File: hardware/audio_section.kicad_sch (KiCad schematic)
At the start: 15 parts, among them J5 AudioJack3_SwitchTR, U2 WAU8812, U8 LM4875

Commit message: Finished power section
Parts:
- removed U8: LM4875, Package_SO:SOIC-8_3.9x4.9mm_P1.27mm, symbol newsymbols:LM4875
- added U10: LM4875, Package_SO:SOIC-8_3.9x4.9mm_P1.27mm, symbol additional_symbols:LM4875
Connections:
- net +5V: now also U10.1 (VDD)
- net GND: now also U10.6 (GND)
- net SPEAKER +: now also U10.5 (Vo1)
- net SPEAKER -: now also U10.8 (Vo2)
- net Volume control: now also U10.4 (DC_vol/~{SD})
- net at R11.1, R12.1, R13.1: now also U10.2 (-Vin)
- net at R15.2: now also U10.3 (HP_Sense)
- net at C17.1: now also U10.7 (Bypass)
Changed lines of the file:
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@@
 	)
 	(symbol
-		(lib_id "newsymbols:LM4875")
+		(lib_id "additional_symbols:LM4875")
 		(at 124.46 67.31 0)
 		(unit 1)
@@
 		(on_board yes)
 		(dnp no)
-		(property "Reference" "U8"
-			(at 128.27 64.77 0)
+		(fields_autoplaced yes)
+		(property "Reference" "U10"
+			(at 122.7933 64.77 0)
 			(effects
 				(font
 					(size 1.27 1.27)
 				)
+				(justify left)
 			)
 		)
 		(property "Value" "LM4875"
-			(at 130.81 67.31 0)
+			(at 122.7933 67.31 0)
 			(effects
 				(font
 					(size 1.27 1.27)
 				)
+				(justify left)
 			)
 		)
 		(property "Footprint" "Package_SO:SOIC-8_3.9x4.9mm_P1.27mm"
-			(at 124.46 64.77 0)
+			(at 121.158 49.53 0)
 			(effects
 				(font
@@
 		)
 		(property "Datasheet" "https://www.ti.com/lit/ds/symlink/lm4875.pdf"
-			(at 124.46 62.23 0)
+			(at 121.158 46.99 0)
 			(effects
 				(font
@@
 			)
 		)
-		(property "Description" ""
-			(at 124.46 67.31 0)
+		(property "Description" "750 mW Audio Power Amplifier with DC Volume Control and Headphone Switch"
+			(at 121.158 52.07 0)
 			(effects
 				(font
 					(size 1.27 1.27)
 				)
+				(hide yes)
 			)
 		)
-		(pin "4"
+		(pin "5"
+		)
+		(pin "8"
 		)
 		(pin "3"
-		)
-		(pin "1"
-		)
-		(pin "2"
-		)
-		(pin "5"
 		)
 		(pin "6"
@@
 		(pin "7"
 		)
-		(pin "8"
+		(pin "2"
+		)
+		(pin "4"
+		)
+		(pin "1"
 		)
 		(instances
-			(project "pyheld_pcb"
+			(project ""
 				(path "/ba6f8fdb-f4fe-4618-8996-8010efc6ab22/1cc4485c-21de-4da4-8687-5322240d5e0f"
-					(reference "U8")
+					(reference "U10")
 					(unit 1)
 				)

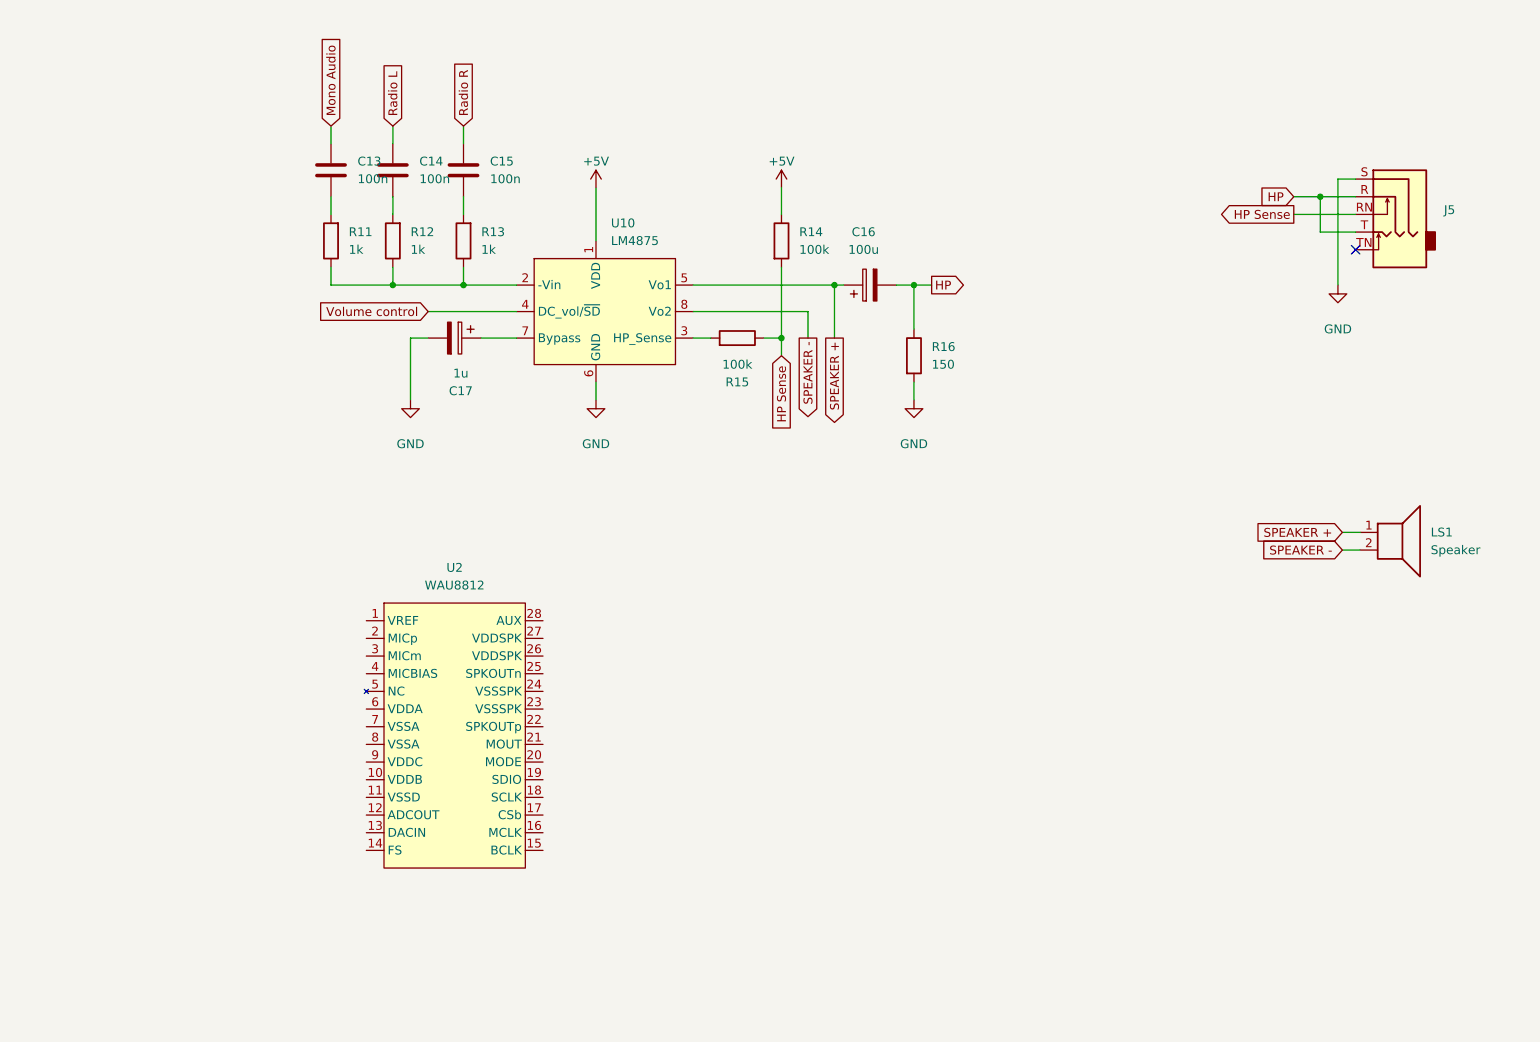
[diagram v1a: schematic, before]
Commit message: Moved MCU to general section
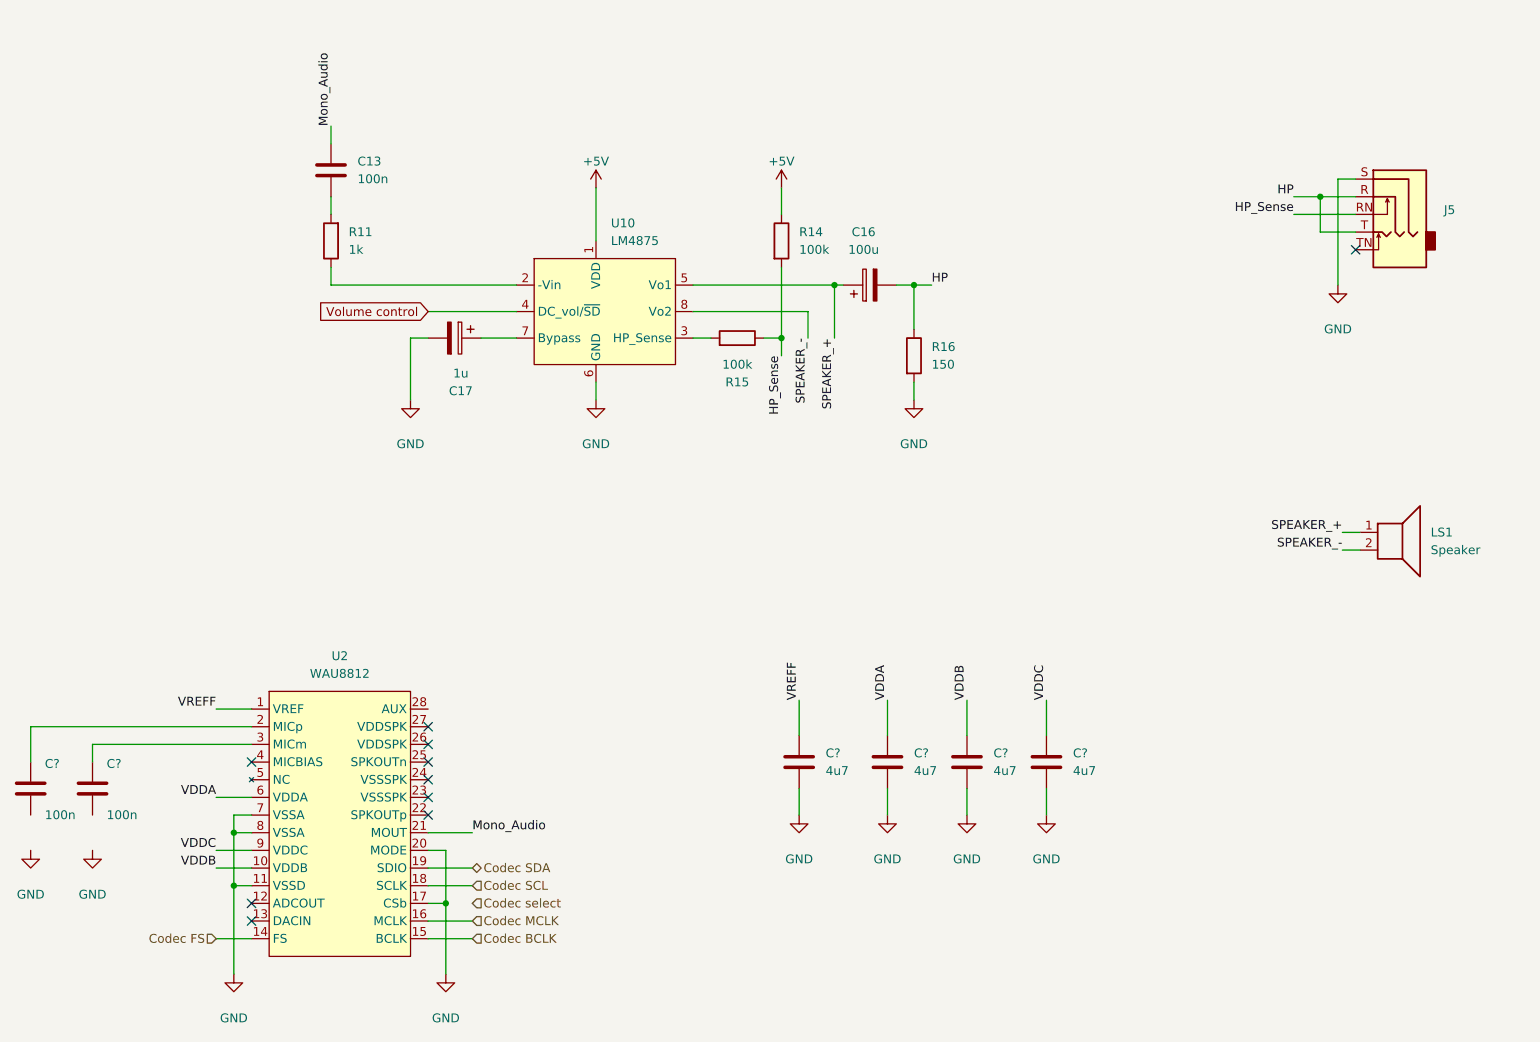
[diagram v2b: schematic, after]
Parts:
- removed C14, C15: 100n, Capacitor_SMD:C_0603_1608Metric, symbol Device:C
- removed R12, R13: 1k, Resistor_SMD:R_0603_1608Metric, symbol Device:R
- added C? (x4): 4u7, Capacitor_SMD:C_0603_1608Metric, symbol Device:C
- added C? (x2): 100n, Capacitor_SMD:C_0603_1608Metric, symbol Device:C
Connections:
- net Mono Audio is gone; now on net Mono_Audio: C13.2
- net GND: now also U2.11 (VSSD), U2.17 (CSb), U2.20 (MODE), U2.7 (VSSA), U2.8 (VSSA), C?.1, C?.1, C?.1, C?.1
- net VREFF: now reaches U2.1 (VREF)
- net VREFF: now also C?.2
- net VDDB: now reaches U2.10 (VDDB)
- net VDDB: now also C?.2
- net Codec FS: now reaches U2.14 (FS)
- net Codec BCLK: now reaches U2.15 (BCLK)
- net Codec MCLK: now reaches U2.16 (MCLK)
- net Codec SCL: now reaches U2.18 (SCLK)
- net Codec SDA: now reaches U2.19 (SDIO)
- net at U2.2 (MICp): now also C?.2
- net Mono_Audio: now reaches U2.21 (MOUT)
- net at U2.3 (MICm): now also C?.2
- net VDDA: now reaches U2.6 (VDDA)
- net VDDA: now also C?.2
- net VDDC: now reaches U2.9 (VDDC)
- net VDDC: now also C?.2
- net HP Sense renamed HP_Sense
- net SPEAKER + renamed SPEAKER_+
- net SPEAKER - renamed SPEAKER_-
- no-connect marks 1 -> 10
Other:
- moved on the sheet: U2

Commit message: Removed additional audio circuits Simplified connections -> change DAC (WAU8812 will be difficult by now to make working)
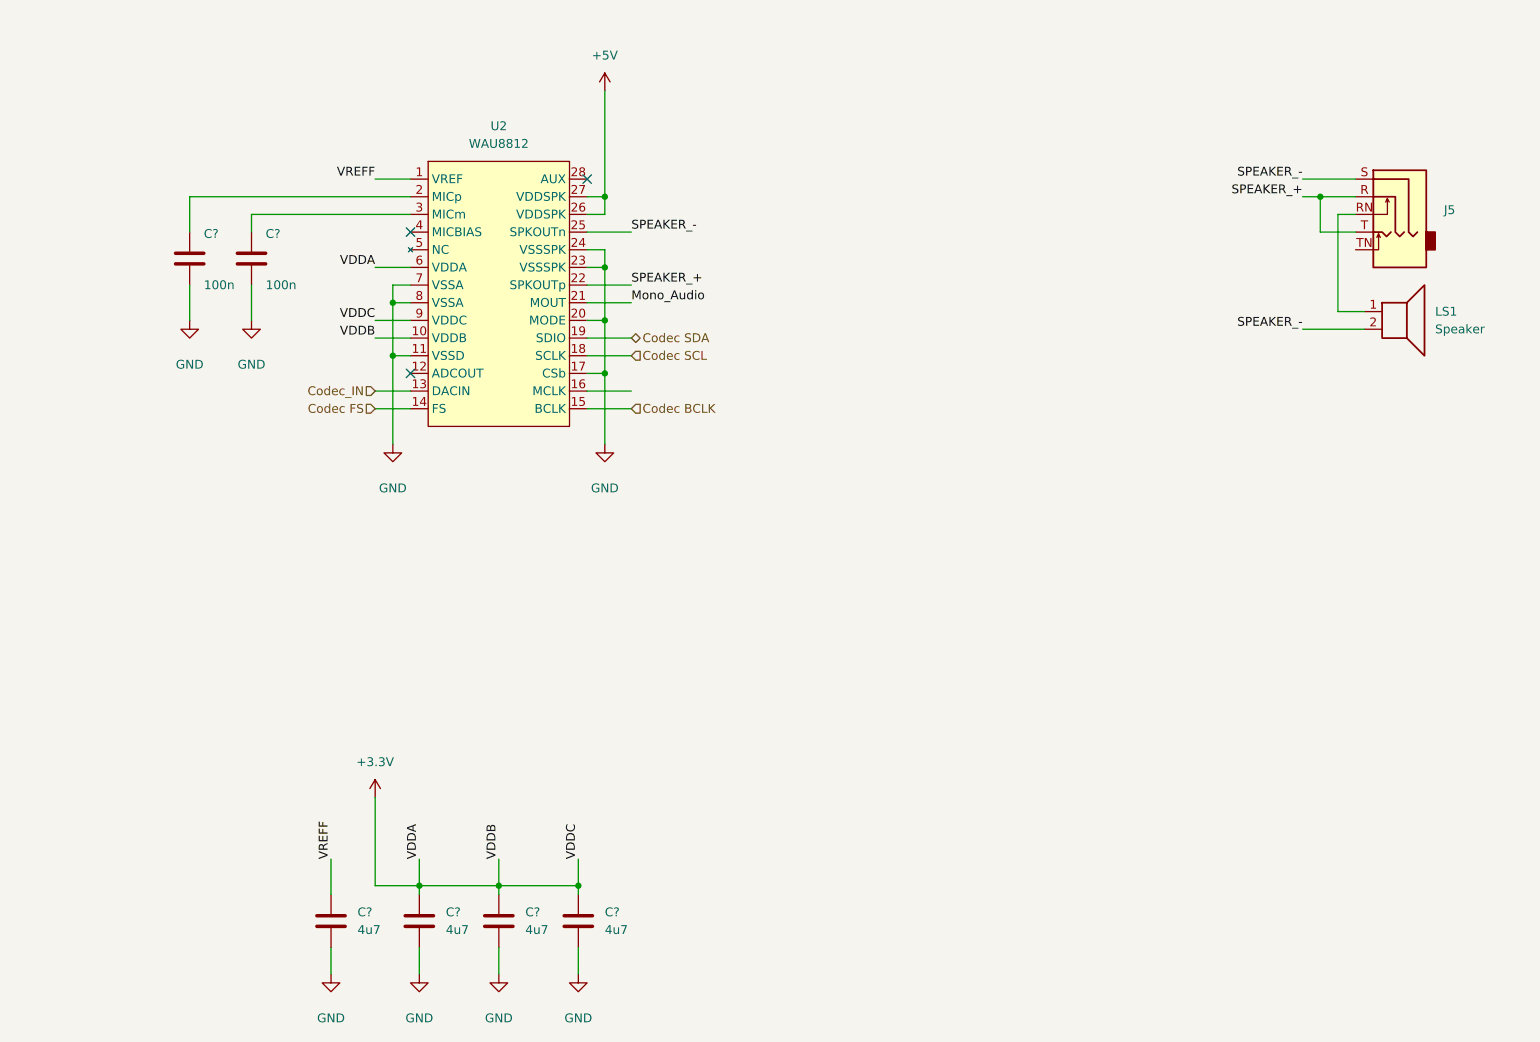
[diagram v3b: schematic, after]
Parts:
- removed C13: 100n, Capacitor_SMD:C_0603_1608Metric, symbol Device:C
- removed C16: 100u, Capacitor_SMD:C_0603_1608Metric, symbol Device:C_Polarized
- removed C17: 1u, Capacitor_SMD:C_0603_1608Metric, symbol Device:C_Polarized
- removed R11: 1k, Resistor_SMD:R_0603_1608Metric, symbol Device:R
- removed R14, R15: 100k, Resistor_SMD:R_0603_1608Metric, symbol Device:R
- removed R16: 150, Resistor_SMD:R_0603_1608Metric, symbol Device:R
- removed U10: LM4875, Package_SO:SOIC-8_3.9x4.9mm_P1.27mm, symbol additional_symbols:LM4875
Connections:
- net HP is gone; now on net SPEAKER_+: J5.R, J5.T
- net VDDB is gone; now on net +3.3V: C?.2, U2.10 (VDDB)
- net VDDC is gone; now on net +3.3V: C?.2, U2.9 (VDDC)
- net +5V: now also U2.26 (VDDSPK), U2.27 (VDDSPK)
- net GND: now also C?.1, C?.1, U2.23 (VSSSPK), U2.24 (VSSSPK); no longer J5.S
- net SPEAKER_+: now also U2.22 (SPKOUTp); no longer LS1.1
- net SPEAKER_-: now also J5.S, U2.25 (SPKOUTn)
- net Codec_IN: now reaches U2.13 (DACIN)
- net Codec MCLK: no longer names the net of U2.16 (MCLK)
- net HP_Sense: no longer names the net of J5.RN
- net HP_Sense: now also LS1.1
- net VDDA renamed +3.3V
- no-connect marks 10 -> 3
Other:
- moved on the sheet: C?, LS1, U2

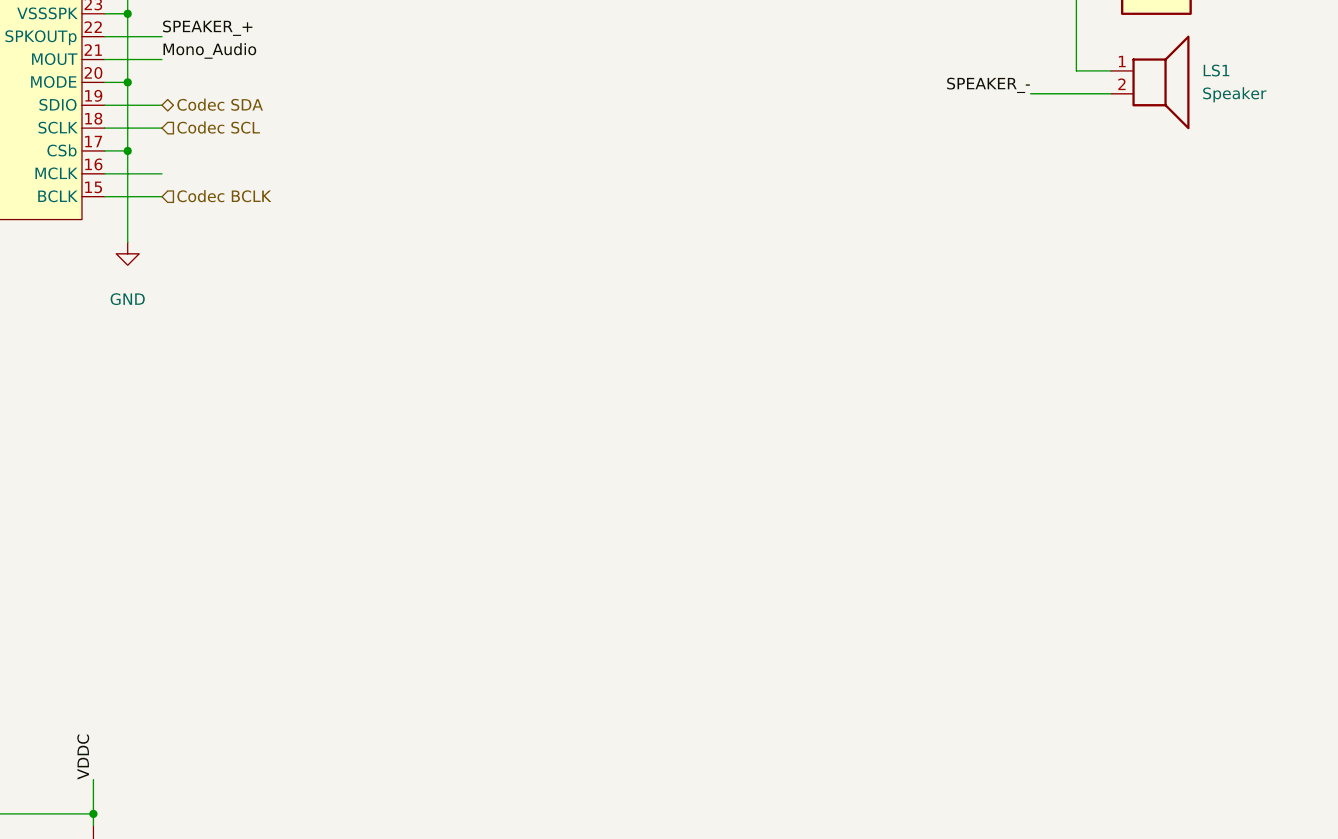
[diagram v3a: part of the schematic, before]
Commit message: added audio module header
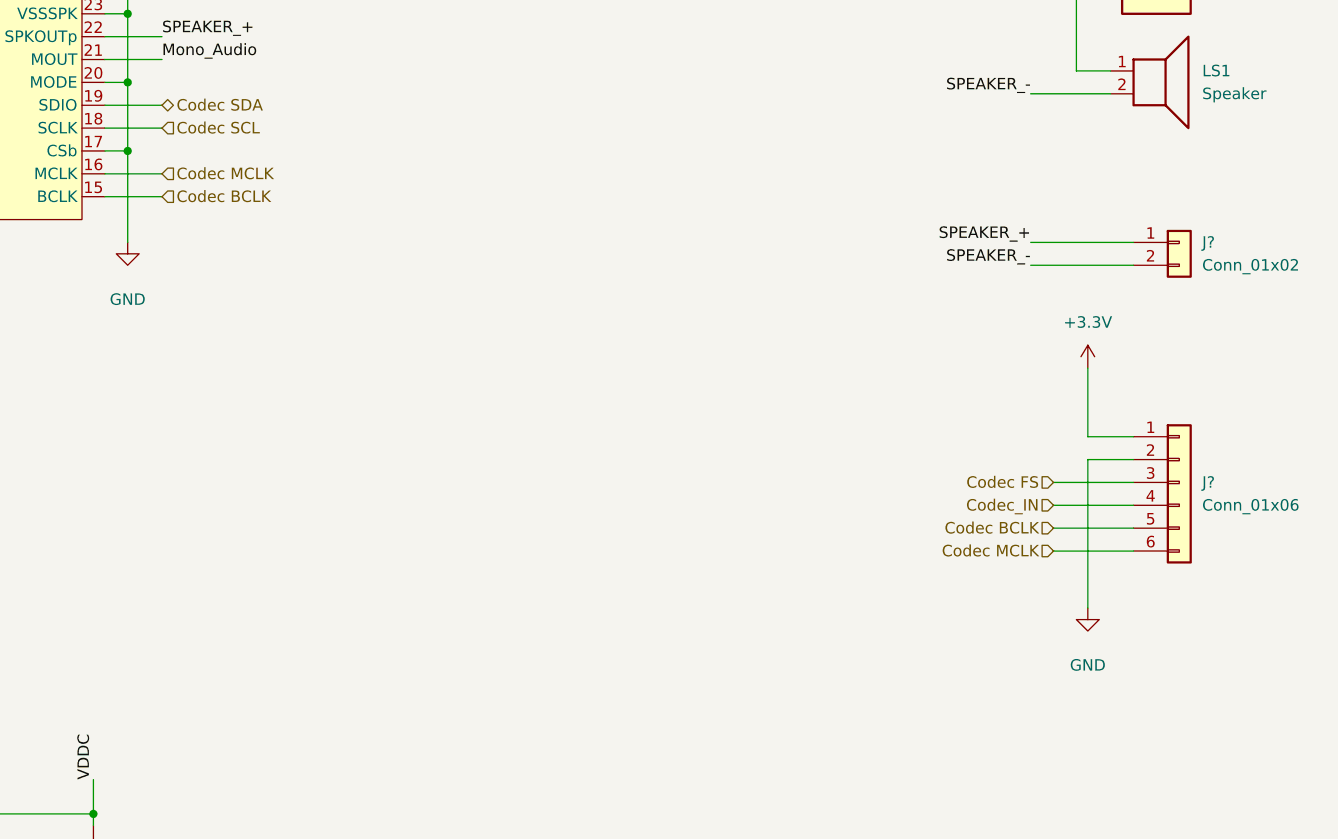
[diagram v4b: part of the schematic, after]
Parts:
- added J?: Conn_01x06, symbol Connector_Generic:Conn_01x06
- added J?: Conn_01x02, symbol Connector_Generic:Conn_01x02
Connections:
- net +3.3V: now also J?.1 (Pin_1)
- net Codec BCLK: now also J?.5 (Pin_5)
- net Codec FS: now also J?.3 (Pin_3)
- net Codec_IN: now also J?.4 (Pin_4)
- net GND: now also J?.2 (Pin_2)
- net SPEAKER_+: now also J?.1 (Pin_1)
- net SPEAKER_-: now also J?.2 (Pin_2)
- net Codec MCLK: now reaches U2.16 (MCLK)
- net Codec MCLK: now also J?.6 (Pin_6)
